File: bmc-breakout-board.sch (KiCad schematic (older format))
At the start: 20 parts, among them J1 PinHeader_2x4, J10 PinHeader_2x4, J11 PinHeader_2x05, J12 61300411121, J13 0473460001, J14 PCIE_BUS_x1, J15 0473460001, J16 PinHeader_1x07, J2 PinHeader_2x13, J3 PinHeader_2x08, J4 61300411121, J5 ME1016813401101, J6 61300411121, J7 DC_SOCKET, J8 PinHeader_2x05, J9 PinHeader_1x07

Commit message: Edit logo
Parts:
- D1, D2: footprint antmicro-footprints:SOT-3 -> bmc-breakout-board-footprints:SOT-3; symbol antmicroTVSDiodes:TPD2E009 -> bmc-breakout-board:TPD2E009
- J1, J10: footprint antmicro-footprints:PinHeader_2x04_P2.54mm_Vertical -> bmc-breakout-board-footprints:PinHeader_2x04_P2.54mm_Vertical; symbol antmicroRectangularConnectorsHeadersMalePins:PinHeader_2x4 -> bmc-breakout-board:PinHeader_2x4
- J11, J8: footprint antmicro-footprints:PinHeader_2x05_P2.54mm_Vertical -> bmc-breakout-board-footprints:PinHeader_2x05_P2.54mm_Vertical; symbol antmicroRectangularConnectorsHeadersMalePins:PinHeader_2x05 -> bmc-breakout-board:PinHeader_2x05
- J12, J4, J6: footprint antmicro-footprints:PinHeader_1x4_P2.54mm_Drill1.02mm -> bmc-breakout-board-footprints:PinHeader_1x4_P2.54mm_Drill1.02mm; symbol antmicroRectangularConnectorsHeadersMalePins:61300411121 -> bmc-breakout-board:61300411121
- J13, J15: footprint antmicro-footprints:USB_Micro_B_Female_0473460001 -> bmc-breakout-board-footprints:USB_Micro_B_Female_0473460001; symbol antmicroUSBDVIHDMIConnectors:0473460001 -> bmc-breakout-board:0473460001
- J14: footprint antmicro-footprints:BUS_PCIexpress_x1 -> bmc-breakout-board-footprints:BUS_PCIexpress_x1; symbol antmicroPciConnectors:PCIE_BUS_x1 -> bmc-breakout-board:PCIE_BUS_x1
- J16, J9: footprint antmicro-footprints:PinHeader_1x07_P2.54mm_Vertical -> bmc-breakout-board-footprints:PinHeader_1x07_P2.54mm_Vertical; symbol antmicroRectangularConnectorsHeadersMalePins:PinHeader_1x07 -> bmc-breakout-board:PinHeader_1x07
- J2: footprint antmicro-footprints:PinHeader_2x13_P2.54mm_Vertical -> bmc-breakout-board-footprints:PinHeader_2x13_P2.54mm_Vertical; symbol antmicroRectangularConnectorsHeadersMalePins:PinHeader_2x13 -> bmc-breakout-board:PinHeader_2x13
- J3: footprint antmicro-footprints:PinHeader_2x08_P2.54mm_Vertical -> bmc-breakout-board-footprints:PinHeader_2x08_P2.54mm_Vertical; symbol antmicroRectangularConnectorsHeadersMalePins:PinHeader_2x08 -> bmc-breakout-board:PinHeader_2x08
- J5: footprint antmicro-footprints:ME1016813401101 -> bmc-breakout-board-footprints:ME1016813401101; symbol antmicroPciConnectors:ME1016813401101 -> bmc-breakout-board:ME1016813401101
- J7: footprint antmicro-footprints:DC_SOCKET -> bmc-breakout-board-footprints:DC_SOCKET; symbol antmicroBarrelAudioConnectors:DC_SOCKET -> bmc-breakout-board:DC_SOCKET
- N1: footprint antmicro-footprints:antmicro-logo_scaled_20mm -> bmc-breakout-board-footprints:antmicro-logo_scaled_20mm_mask; symbol antmicroMechanicalParts:antmicro_logo -> bmc-breakout-board:antmicro_logo
- R1: footprint antmicro-footprints:0402-res -> bmc-breakout-board-footprints:0402-res; symbol antmicroResistors0402:R_0R_0402 -> bmc-breakout-board:R_0R_0402

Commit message: Add a power switch
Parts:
- added Q1: BSS138AKA, bmc-breakout-board-footprints:SOT-23-3, symbol bmc-breakout-board:BSS138AKA
- added R2: R_10k_0402, bmc-breakout-board-footprints:0402-res, symbol bmc-breakout-board:R_10k_0402
- added S1: JS202011SCQN, bmc-breakout-board-footprints:Switch_Slide_JS202011SCQN, symbol bmc-breakout-board:JS202011SCQN
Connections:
- net labels added: P12V_IN
- wire segments 271 -> 289
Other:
- moved on the sheet: J7
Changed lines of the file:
@@
 L bmc-breakout-board:DC_SOCKET J7
 U 1 1 6074EED5
-P 7950 1550
-F 0 "J7" H 7572 1611 60  0000 R CNN
-F 1 "DC_SOCKET" H 8000 1275 60  0001 C CNN
-F 2 "bmc-breakout-board-footprints:DC_SOCKET" H 8000 1200 60  0001 C CNN
-F 3 "" H 7950 1550 60  0001 C CNN
-F 4 "Multicomp" H 7975 1075 50  0001 C CNN "Manufacturer"
-F 5 "MJ-179PH" H 7572 1513 50  0000 R CNN "MPN"
-	1    7950 1550
+P 11675 6025
+F 0 "J7" H 11297 6086 60  0000 R CNN
+F 1 "DC_SOCKET" H 11725 5750 60  0001 C CNN
+F 2 "bmc-breakout-board-footprints:DC_SOCKET" H 11725 5675 60  0001 C CNN
+F 3 "" H 11675 6025 60  0001 C CNN
+F 4 "Multicomp" H 11700 5550 50  0001 C CNN "Manufacturer"
+F 5 "MJ-179PH" H 11297 5988 50  0000 R CNN "MPN"
+	1    11675 6025
 	-1   0    0    -1
 $EndComp
-Text GLabel 7750 1450 0    50   Input ~ 0
-P12V_AUX
-Wire Wire Line
-	7750 1550 7750 1650
-Connection ~ 7750 1650
-Wire Wire Line
-	7750 1650 7750 1825
+Text GLabel 11475 5925 0    50   Input ~ 0
+P12V_IN
+Wire Wire Line
+	11475 6025 11475 6125
+Connection ~ 11475 6125
+Wire Wire Line
+	11475 6125 11475 6300
 $Comp
 L bmc-breakout-board:61300411121 J6
@@
 L bmc-breakout-board:GND #PWR0109
 U 1 1 60323931
-P 7750 1825
-F 0 "#PWR0109" H 7750 1575 50  0001 C CNN
-F 1 "GND" H 7755 1652 50  0000 C CNN
-F 2 "" H 7750 1825 50  0001 C CNN
-F 3 "" H 7750 1825 50  0001 C CNN
-	1    7750 1825
-	1    0    0    -1
-$EndComp
+P 11475 6300
+F 0 "#PWR0109" H 11475 6050 50  0001 C CNN
+F 1 "GND" H 11480 6127 50  0000 C CNN
+F 2 "" H 11475 6300 50  0001 C CNN
+F 3 "" H 11475 6300 50  0001 C CNN
+	1    11475 6300
+	1    0    0    -1
+$EndComp
+Text GLabel 12875 5525 1    50   Input ~ 0
+P12V_IN
+$Comp
+L bmc-breakout-board:R_10k_0402 R2
+U 1 1 60CBB640
+P 12875 5850
+F 0 "R2" V 12830 5920 60  0000 L CNN
+F 1 "R_10k_0402" H 12875 5700 60  0001 C CNN
+F 2 "bmc-breakout-board-footprints:0402-res" H 13075 6050 60  0001 L CNN
+F 3 "" H 12875 5850 50  0001 C CNN
+F 4 "VISHAY" H 13075 6250 60  0001 L CNN "Manufacturer"
+F 5 "CRCW040210K0FKEDHP" H 13075 6150 60  0001 L CNN "MPN"
+F 6 "10k" V 12928 5920 50  0000 L CNN "Val"
+	1    12875 5850
+	0    -1   1    0
+$EndComp
+Wire Wire Line
+	12875 5525 12875 5700
+Wire Wire Line
+	13000 6250 13000 6650
+$Comp
+L bmc-breakout-board:GND #PWR0110
+U 1 1 60D4DCD1
+P 13000 6950
+F 0 "#PWR0110" H 13000 6700 50  0001 C CNN
+F 1 "GND" H 13005 6777 50  0000 C CNN
+F 2 "" H 13000 6950 50  0001 C CNN
+F 3 "" H 13000 6950 50  0001 C CNN
+	1    13000 6950
+	1    0    0    -1
+$EndComp
+Wire Wire Line
+	13000 6250 13125 6250
+Text GLabel 14425 5500 1    50   Input ~ 0
+P12V_AUX
+Wire Wire Line
+	14425 5750 14425 5500
+$Comp
+L bmc-breakout-board:BSS138AKA Q1
+U 1 1 60C594B1
+P 13975 5750
+F 0 "Q1" H 14083 5803 60  0000 L CNN
+F 1 "BSS138AKA" H 14083 5697 60  0000 L CNN
+F 2 "bmc-breakout-board-footprints:SOT-23-3" H 14175 5950 60  0001 L CNN
+F 3 "https://www.onsemi.com/pub/Collateral/BSS138-D.PDF" H 14175 6050 60  0001 L CNN
+F 4 "BSS138AKAR" H 14175 6250 60  0001 L CNN "MPN"
+F 5 "ON Semiconductor" H 14175 6850 60  0001 L CNN "Manufacturer"
+	1    13975 5750
+	0    -1   -1   0
+$EndComp
+Wire Wire Line
+	13500 5750 13500 5500
+Text GLabel 13500 5500 1    50   Input ~ 0
+P12V_IN
+Wire Wire Line
+	13500 5750 13775 5750
+Wire Wire Line
+	14175 5750 14425 5750
+Wire Wire Line
+	14075 6150 14075 6050
+Wire Wire Line
+	13525 6150 13650 6150
+$Comp
+L bmc-breakout-board:JS202011SCQN S1
+U 1 1 60EE970A
+P 13325 6350
+F 0 "S1" H 13325 5825 50  0000 C CNN
+F 1 "JS202011SCQN" H 13325 5916 50  0000 C CNN
+F 2 "bmc-breakout-board-footprints:Switch_Slide_JS202011SCQN" H 13525 6550 50  0001 L CNN
+F 3 "https://www.ckswitches.com/media/1422/js.pdf" H 13525 6650 60  0001 L CNN
+F 4 "JS202011SCQN" H 13525 6850 60  0001 L CNN "MPN"
+F 5 "C&K" H 13525 7450 60  0001 L CNN "Manufacturer"
+	1    13325 6350
+	-1   0    0    1
+$EndComp
+Wire Wire Line
+	13000 6650 13125 6650
+Connection ~ 13000 6650
+Wire Wire Line
+	13000 6650 13000 6950
+Wire Wire Line
+	13125 6450 12875 6450
+Wire Wire Line
+	12875 6450 12875 6050
+Connection ~ 12875 6050
+Wire Wire Line
+	12875 6050 12875 6000
+Wire Wire Line
+	13125 6050 12875 6050
+Wire Wire Line
+	13525 6550 13650 6550
+Wire Wire Line
+	13650 6550 13650 6150
+Connection ~ 13650 6150
+Wire Wire Line
+	13650 6150 14075 6150
 $EndSCHEMATC

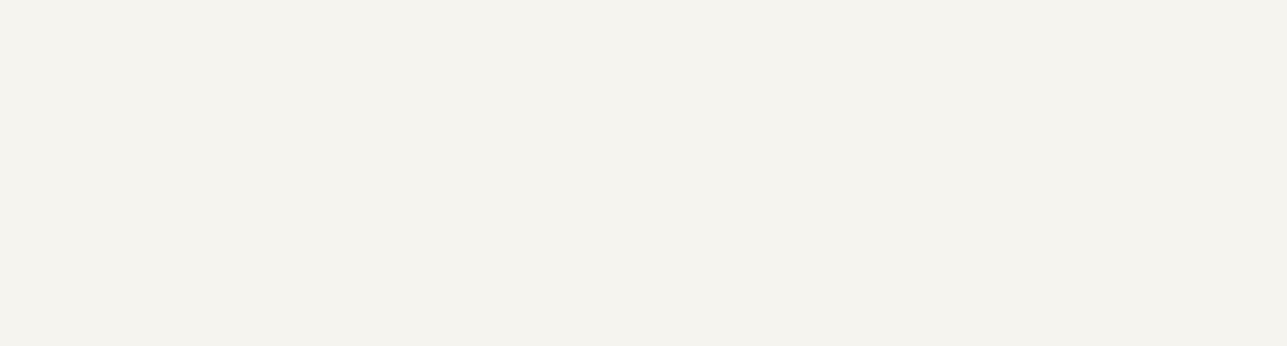
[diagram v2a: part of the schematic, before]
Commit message: Add mounting holes
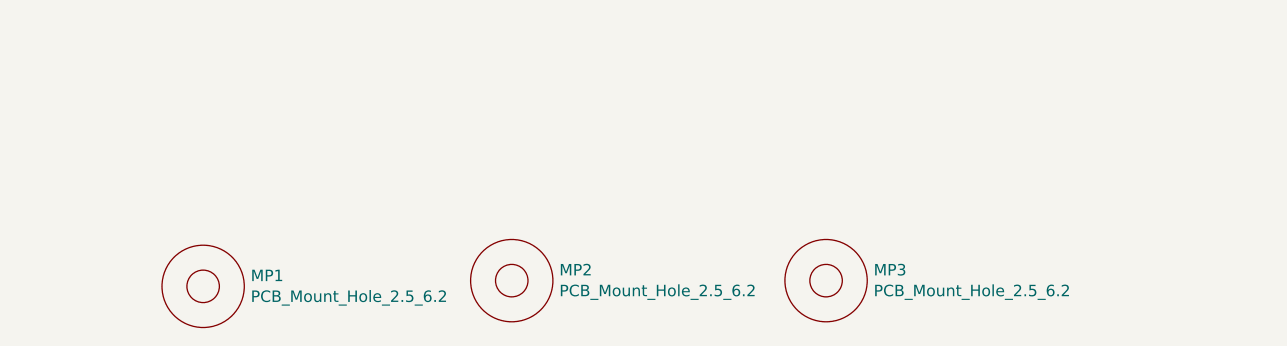
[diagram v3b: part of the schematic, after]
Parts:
- added MP1, MP2, MP3: PCB_Mount_Hole_2.5_6.2, bmc-breakout-board-footprints:Mount-hole-M2.5, symbol bmc-breakout-board:PCB_Mount_Hole_2.5_6.2
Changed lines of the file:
@@
 Wire Wire Line
 	13650 6150 14075 6150
+$Comp
+L bmc-breakout-board:PCB_Mount_Hole_2.5_6.2 MP2
+U 1 1 6105A94D
+P 9150 10825
+F 0 "MP2" H 9358 10871 50  0000 L CNN
+F 1 "PCB_Mount_Hole_2.5_6.2" H 9358 10780 50  0000 L CNN
+F 2 "bmc-breakout-board-footprints:Mount-hole-M2.5" H 9950 11525 50  0001 C CNN
+F 3 "" H 10100 11625 50  0001 C CNN
+	1    9150 10825
+	1    0    0    -1
+$EndComp
+$Comp
+L bmc-breakout-board:PCB_Mount_Hole_2.5_6.2 MP3
+U 1 1 6105ADF7
+P 10525 10825
+F 0 "MP3" H 10733 10871 50  0000 L CNN
+F 1 "PCB_Mount_Hole_2.5_6.2" H 10733 10780 50  0000 L CNN
+F 2 "bmc-breakout-board-footprints:Mount-hole-M2.5" H 11325 11525 50  0001 C CNN
+F 3 "" H 11475 11625 50  0001 C CNN
+	1    10525 10825
+	1    0    0    -1
+$EndComp
+$Comp
+L bmc-breakout-board:PCB_Mount_Hole_2.5_6.2 MP1
+U 1 1 6105B178
+P 7800 10850
+F 0 "MP1" H 8008 10896 50  0000 L CNN
+F 1 "PCB_Mount_Hole_2.5_6.2" H 8008 10805 50  0000 L CNN
+F 2 "bmc-breakout-board-footprints:Mount-hole-M2.5" H 8600 11550 50  0001 C CNN
+F 3 "" H 8750 11650 50  0001 C CNN
+	1    7800 10850
+	1    0    0    -1
+$EndComp
 $EndSCHEMATC

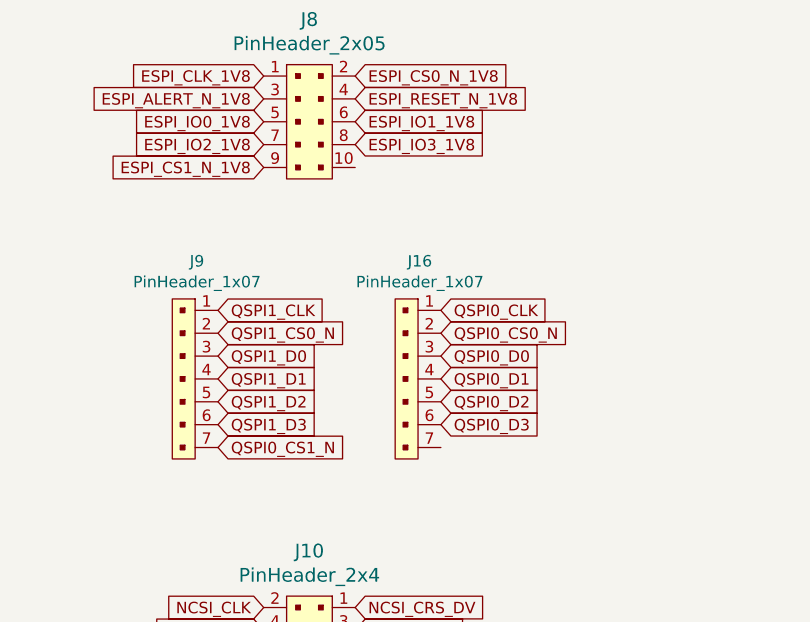
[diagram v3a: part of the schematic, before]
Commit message: Add descriptions on the silkscreen layer
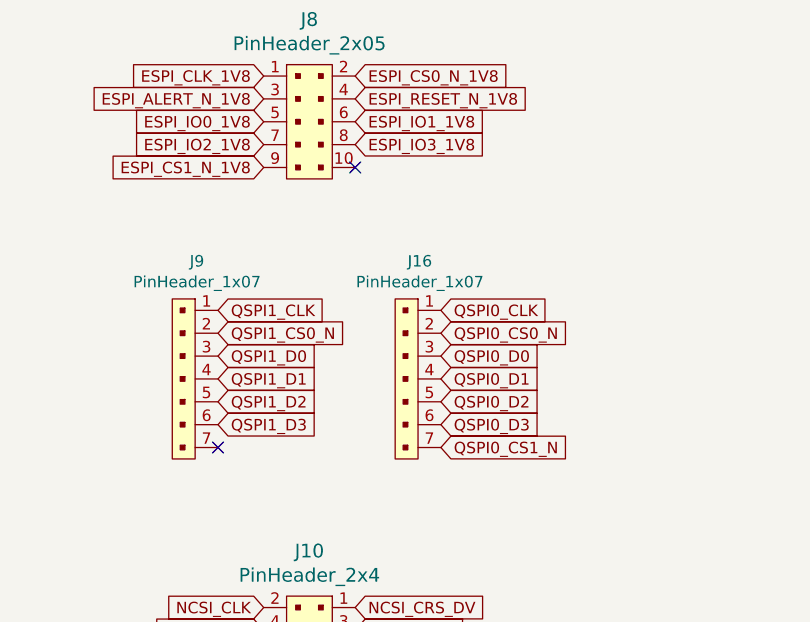
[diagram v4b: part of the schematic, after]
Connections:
- no-connect marks 14 -> 16
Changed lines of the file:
@@
 Text GLabel 8875 7050 2    50   Input ~ 0
 RSVD2
-Text GLabel 8325 4950 2    50   Input ~ 0
+Text GLabel 9300 4950 2    50   Input ~ 0
 QSPI0_CS1_N
 Text GLabel 1650 7925 2    50   Input ~ 0
@@
 	1    0    0    -1
 $EndComp
+NoConn ~ 8325 4950
+NoConn ~ 8925 3725
 $EndSCHEMATC

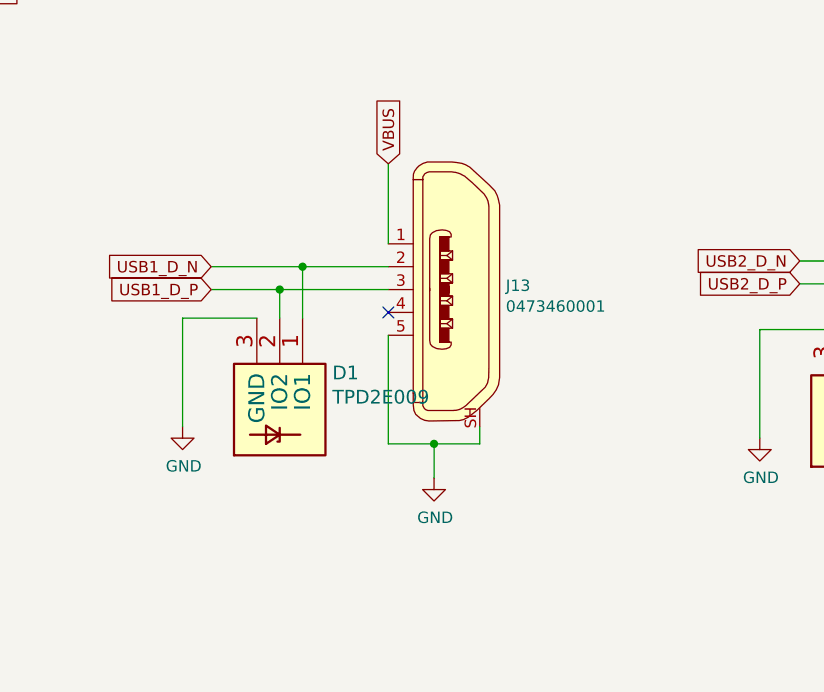
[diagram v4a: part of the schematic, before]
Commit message: Replace host USB with USB A
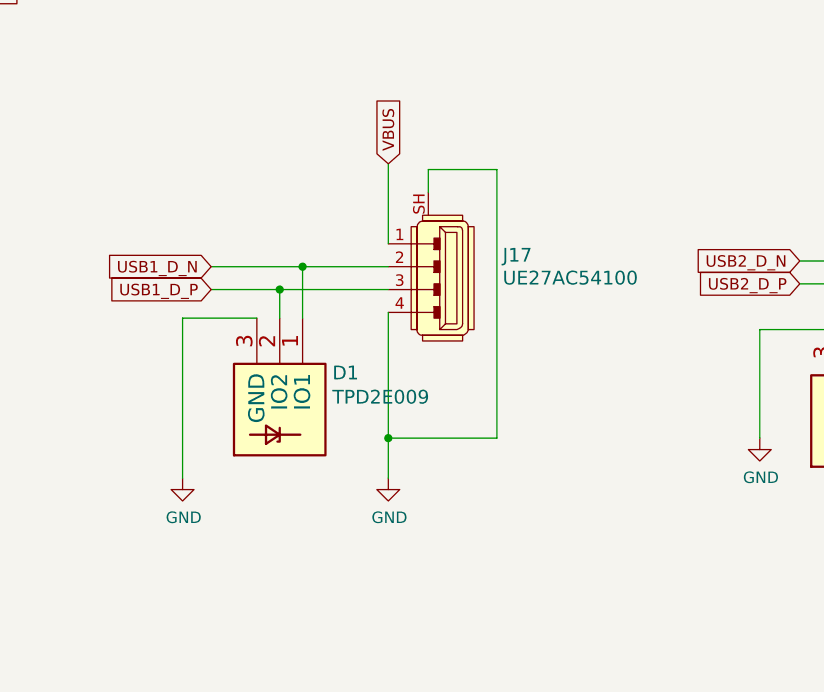
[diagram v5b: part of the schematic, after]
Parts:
- removed J13: 0473460001, bmc-breakout-board-footprints:USB_Micro_B_Female_0473460001, symbol bmc-breakout-board:0473460001
- added J17: UE27AC54100, bmc-breakout-board-footprints:USB_A_Female_UE27AC54100, symbol bmc-breakout-board:UE27AC54100
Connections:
- wire segments 289 -> 290
- no-connect marks 16 -> 15
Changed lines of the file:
@@
 NoConn ~ 12625 3625
 NoConn ~ 12625 4125
-$Comp
-L bmc-breakout-board:0473460001 J15
-U 1 1 6102F623
-P 13825 8225
-F 0 "J15" H 13611 8242 50  0000 R CNN
-F 1 "0473460001" H 13611 8151 50  0000 R CNN
-F 2 "bmc-breakout-board-footprints:USB_Micro_B_Female_0473460001" H 14025 8425 60  0001 L CNN
-F 3 "https://www.molex.com/pdm_docs/sd/473460001_sd.pdf" H 14025 8525 60  0001 L CNN
-F 4 "0473460001" H 14025 8725 60  0001 L CNN "MPN"
-F 5 "Molex" H 14025 9325 60  0001 L CNN "Manufacturer"
-	1    13825 8225
-	-1   0    0    -1
-$EndComp
-$Comp
-L bmc-breakout-board:0473460001 J13
-U 1 1 61030069
-P 11250 8250
-F 0 "J13" H 11036 8267 50  0000 R CNN
-F 1 "0473460001" H 11036 8176 50  0000 R CNN
-F 2 "bmc-breakout-board-footprints:USB_Micro_B_Female_0473460001" H 11450 8450 60  0001 L CNN
-F 3 "https://www.molex.com/pdm_docs/sd/473460001_sd.pdf" H 11450 8550 60  0001 L CNN
-F 4 "0473460001" H 11450 8750 60  0001 L CNN "MPN"
-F 5 "Molex" H 11450 9350 60  0001 L CNN "Manufacturer"
-	1    11250 8250
-	-1   0    0    -1
-$EndComp
 Wire Wire Line
 	13525 8125 13100 8125
@@
 Wire Wire Line
 	10950 8250 10475 8250
-Wire Wire Line
-	10950 8450 10950 8925
-Wire Wire Line
-	10950 8925 11150 8925
-Wire Wire Line
-	11350 8925 11350 8850
-Wire Wire Line
-	11150 8925 11150 9075
-Connection ~ 11150 8925
-Wire Wire Line
-	11150 8925 11350 8925
-Wire Wire Line
-	13525 8425 13525 8900
-Wire Wire Line
-	13525 8900 13725 8900
-Wire Wire Line
-	13925 8900 13925 8825
-Wire Wire Line
-	13725 8900 13725 9050
-Connection ~ 13725 8900
-Wire Wire Line
-	13725 8900 13925 8900
-NoConn ~ 13525 8325
-NoConn ~ 10950 8350
 Wire Wire Line
 	13525 8025 13525 7675
@@
 	10375 8375 10050 8375
 Wire Wire Line
-	10050 8375 10050 8850
+	10050 8375 10050 9075
 $Comp
 L bmc-breakout-board:PinHeader_2x4 J1
@@
 L bmc-breakout-board:GND #PWR0101
 U 1 1 603085E5
-P 10050 8850
-F 0 "#PWR0101" H 10050 8600 50  0001 C CNN
-F 1 "GND" H 10055 8677 50  0000 C CNN
-F 2 "" H 10050 8850 50  0001 C CNN
-F 3 "" H 10050 8850 50  0001 C CNN
-	1    10050 8850
+P 10050 9075
+F 0 "#PWR0101" H 10050 8825 50  0001 C CNN
+F 1 "GND" H 10055 8902 50  0000 C CNN
+F 2 "" H 10050 9075 50  0001 C CNN
+F 3 "" H 10050 9075 50  0001 C CNN
+	1    10050 9075
 	1    0    0    -1
 $EndComp
@@
 L bmc-breakout-board:GND #PWR0102
 U 1 1 6030A505
-P 11150 9075
-F 0 "#PWR0102" H 11150 8825 50  0001 C CNN
-F 1 "GND" H 11155 8902 50  0000 C CNN
-F 2 "" H 11150 9075 50  0001 C CNN
-F 3 "" H 11150 9075 50  0001 C CNN
-	1    11150 9075
+P 10950 9075
+F 0 "#PWR0102" H 10950 8825 50  0001 C CNN
+F 1 "GND" H 10955 8902 50  0000 C CNN
+F 2 "" H 10950 9075 50  0001 C CNN
+F 3 "" H 10950 9075 50  0001 C CNN
+	1    10950 9075
 	1    0    0    -1
 $EndComp
@@
 F 3 "" H 12575 8900 50  0001 C CNN
 	1    12575 8900
-	1    0    0    -1
-$EndComp
-$Comp
-L bmc-breakout-board:GND #PWR0106
-U 1 1 6031DAB7
-P 13725 9050
-F 0 "#PWR0106" H 13725 8800 50  0001 C CNN
-F 1 "GND" H 13730 8877 50  0000 C CNN
-F 2 "" H 13725 9050 50  0001 C CNN
-F 3 "" H 13725 9050 50  0001 C CNN
-	1    13725 9050
 	1    0    0    -1
 $EndComp
@@
 NoConn ~ 8325 4950
 NoConn ~ 8925 3725
+Wire Wire Line
+	13525 8900 13725 8900
+$Comp
+L bmc-breakout-board:GND #PWR0106
+U 1 1 6031DAB7
+P 13725 9050
+F 0 "#PWR0106" H 13725 8800 50  0001 C CNN
+F 1 "GND" H 13730 8877 50  0000 C CNN
+F 2 "" H 13725 9050 50  0001 C CNN
+F 3 "" H 13725 9050 50  0001 C CNN
+	1    13725 9050
+	1    0    0    -1
+$EndComp
+Wire Wire Line
+	13725 8900 13725 9050
+Connection ~ 13725 8900
+Wire Wire Line
+	13725 8900 13925 8900
+Wire Wire Line
+	13925 8900 13925 8825
+Wire Wire Line
+	13525 8425 13525 8900
+NoConn ~ 13525 8325
+$Comp
+L bmc-breakout-board:UE27AC54100 J17
+U 1 1 60D2ABC3
+P 11250 8150
+F 0 "J17" H 11050 8100 60  0000 R CNN
+F 1 "UE27AC54100" H 11050 8200 60  0000 R CNN
+F 2 "bmc-breakout-board-footprints:USB_A_Female_UE27AC54100" H 11450 8350 60  0001 L CNN
+F 3 "https://www.amphenolcanada.com/ProductSearch/drawings/AC/UE27ACX4X0X.pdf" H 11450 8450 60  0001 L CNN
+F 4 "UE27AC54100" H 11450 8650 60  0001 L CNN "MPN"
+F 5 "Amphenol ICC (Commercial Products)" H 11450 9250 60  0001 L CNN "Manufacturer"
+	1    11250 8150
+	-1   0    0    1
+$EndComp
+$Comp
+L bmc-breakout-board:0473460001 J15
+U 1 1 6102F623
+P 13825 8225
+F 0 "J15" H 13611 8242 50  0000 R CNN
+F 1 "0473460001" H 13611 8151 50  0000 R CNN
+F 2 "bmc-breakout-board-footprints:USB_Micro_B_Female_0473460001" H 14025 8425 60  0001 L CNN
+F 3 "https://www.molex.com/pdm_docs/sd/473460001_sd.pdf" H 14025 8525 60  0001 L CNN
+F 4 "0473460001" H 14025 8725 60  0001 L CNN "MPN"
+F 5 "Molex" H 14025 9325 60  0001 L CNN "Manufacturer"
+	1    13825 8225
+	-1   0    0    -1
+$EndComp
+Wire Wire Line
+	10950 8350 10950 8900
+Wire Wire Line
+	10950 8900 11425 8900
+Wire Wire Line
+	11425 8900 11425 7725
+Wire Wire Line
+	11425 7725 11125 7725
+Wire Wire Line
+	11125 7725 11125 7825
+Connection ~ 10950 8900
+Wire Wire Line
+	10950 8900 10950 9075
 $EndSCHEMATC
